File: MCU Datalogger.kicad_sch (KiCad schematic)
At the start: 25 parts, among them U1 24LC1025, U2 24LC1025, U3 DS1337S_, U4 ATMEGA328P-AU, Y1 16 MHz, Y2 32.768kHz

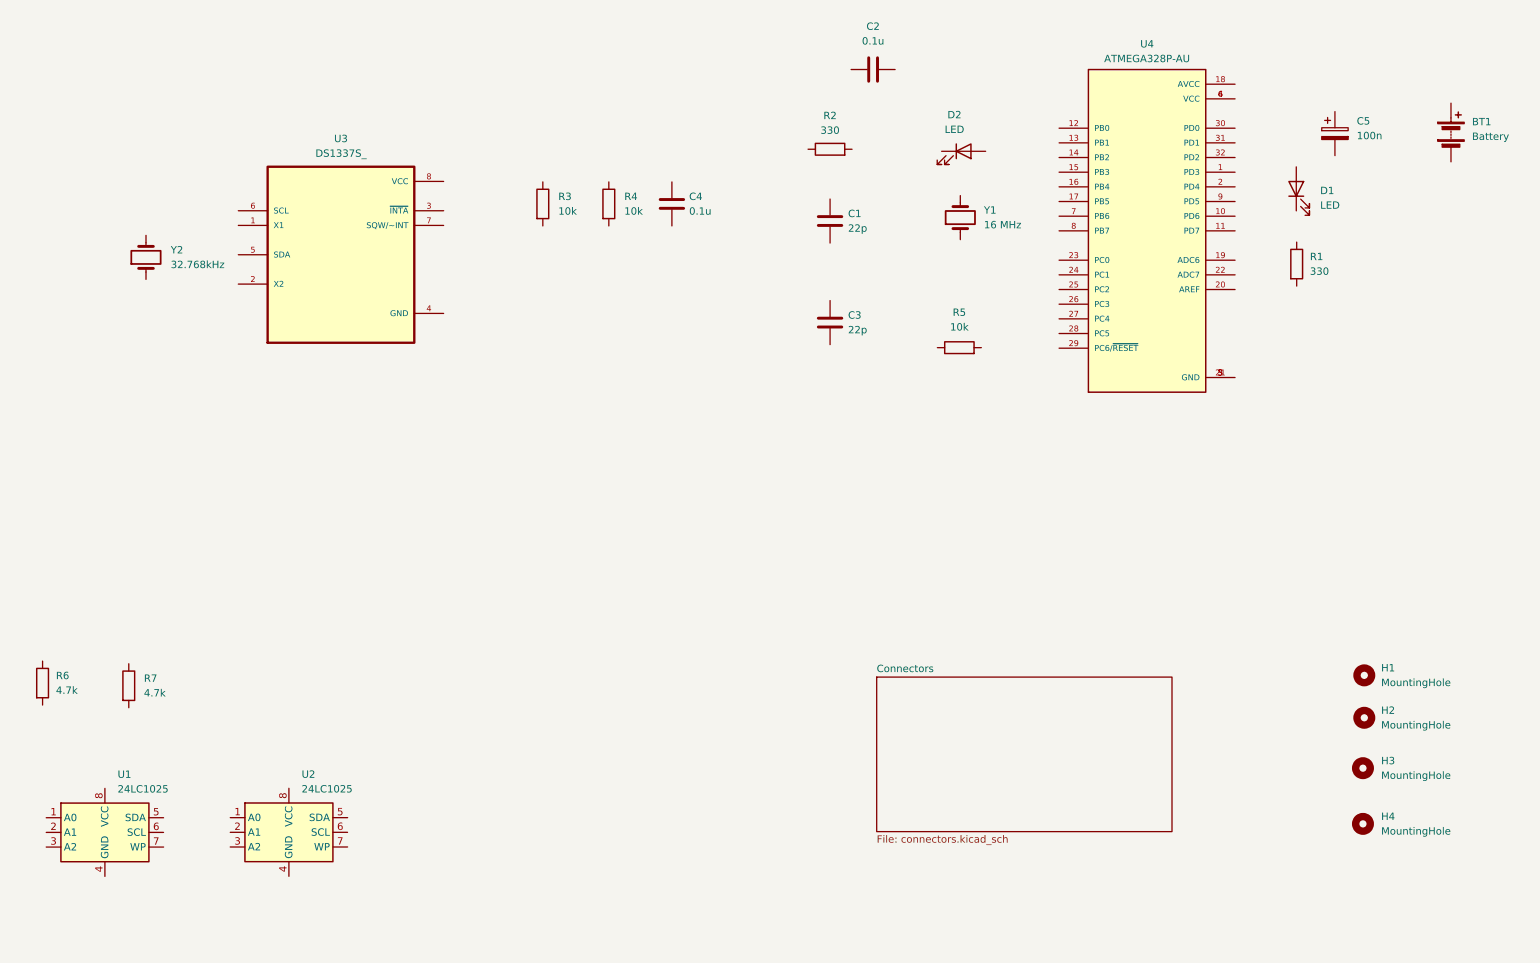
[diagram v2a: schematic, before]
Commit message: completed wiring of main sheet
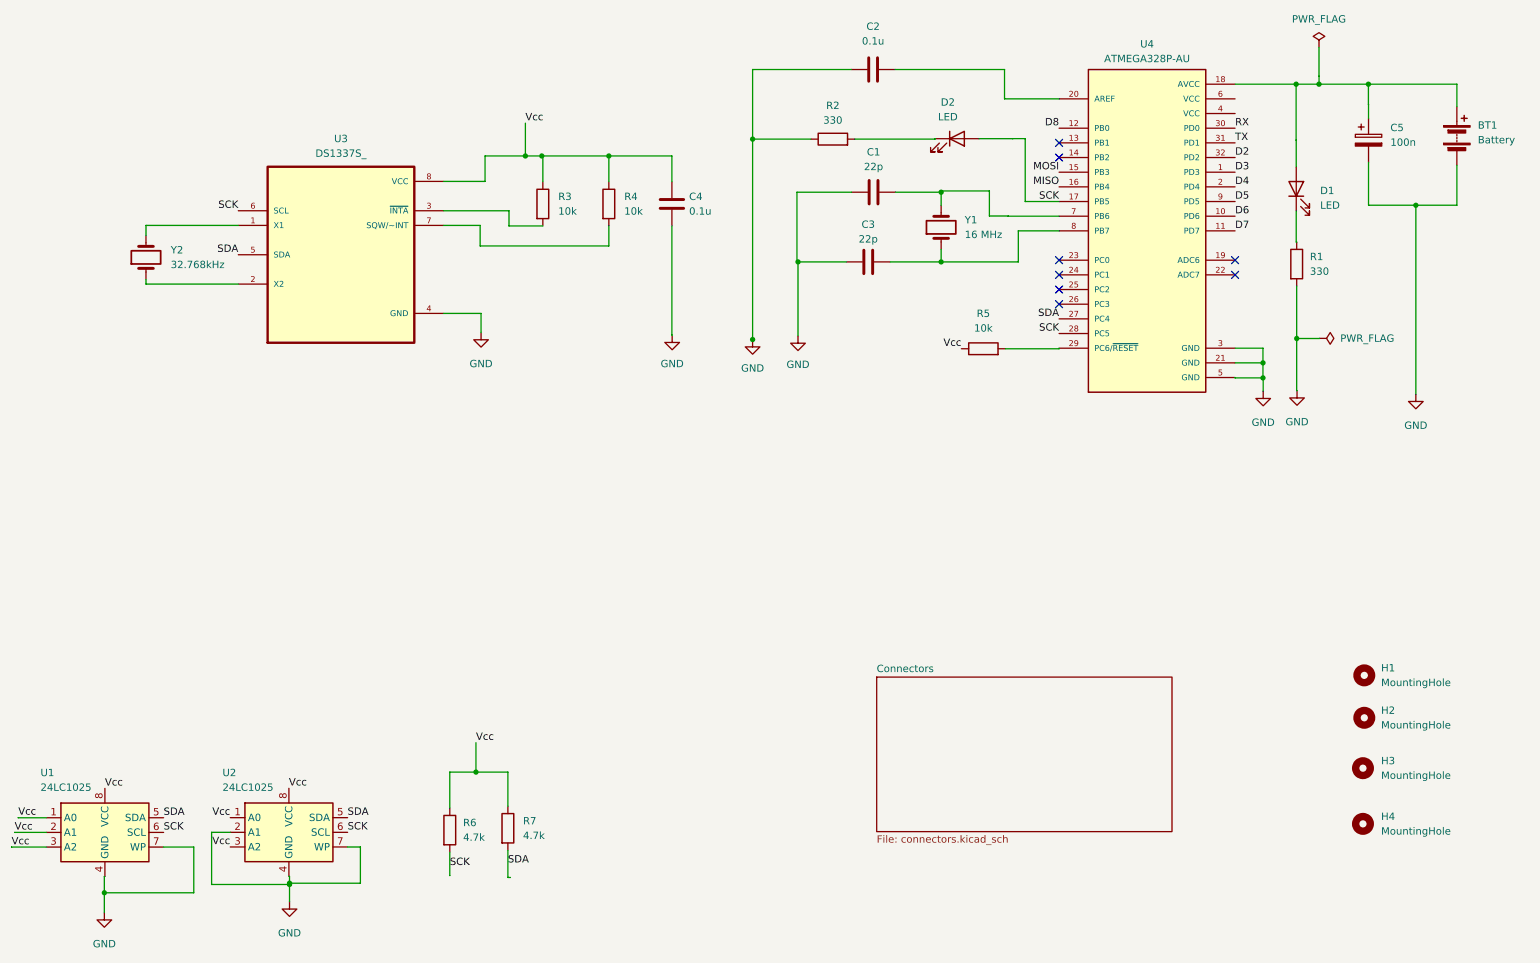
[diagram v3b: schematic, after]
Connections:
- net Vcc: now reaches R7.1
- net Vcc: now also C4.2, R3.1, R4.1, R5.1, R6.1, U1.1 (A0), U1.2 (A1), U1.3 (A2), U1.8 (VCC), U2.1 (A0), U2.3 (A2), U2.8 (VCC), U3.8 (VCC)
- net SDA: now reaches R7.2
- net SDA: now also U1.5 (SDA), U2.5 (SDA), U3.5 (SDA), U4.27 (PC4)
- net at R3.2: now also U3.3 (~{INTA})
- net GND: now reaches C1.1
- net GND: now also BT1.2 (-), C2.1, C3.1, C4.1, C5.2, R1.2, R2.1, U1.4 (GND), U1.7 (WP), U2.2 (A1), U2.4 (GND), U2.7 (WP), U3.4 (GND), U4.3 (GND), U4.5 (GND)
- net at C1.2: now also U4.7 (PB6), Y1.2
- net at C5.1: now also BT1.1 (+), D1.2 (A), U4.18 (AVCC)
- net at R1.1: now also D1.1 (K)
- net at R2.2: now also D2.1 (K)
- net SCK: now reaches U2.6 (SCL)
- net SCK: now also D2.2 (A), R6.2, U1.6 (SCL), U3.6 (SCL), U4.17 (PB5), U4.28 (PC5)
- net at R4.2: now also U3.7 (SQW/~INT)
- net at C3.2: now also U4.8 (PB7), Y1.1
- net at R5.2: now also U4.29 (PC6/~{RESET})
- net at C2.2: now also U4.20 (AREF)
- net at U3.1 (X1): now also Y2.2
- net at U3.2 (X2): now also Y2.1
- net D3: now reaches U4.1 (PD3)
- net D6: now reaches U4.10 (PD6)
- net D7: now reaches U4.11 (PD7)
- net D8: now reaches U4.12 (PB0)
- net MOSI: now reaches U4.15 (PB3)
- net MISO: now reaches U4.16 (PB4)
- net D4: now reaches U4.2 (PD4)
- net RX: now reaches U4.30 (PD0)
- net TX: now reaches U4.31 (PD1)
- net D2: now reaches U4.32 (PD2)
- net at U4.4 (VCC): no longer U4.6 (VCC)
- net D5: now reaches U4.9 (PD5)
- now unconnected: U4.21 (GND)
- no-connect marks 0 -> 8
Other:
- moved on the sheet: BT1, C1, C3, C5, D2, R2, R5, R6, R7, Y1

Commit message: Completed wiring in schematic
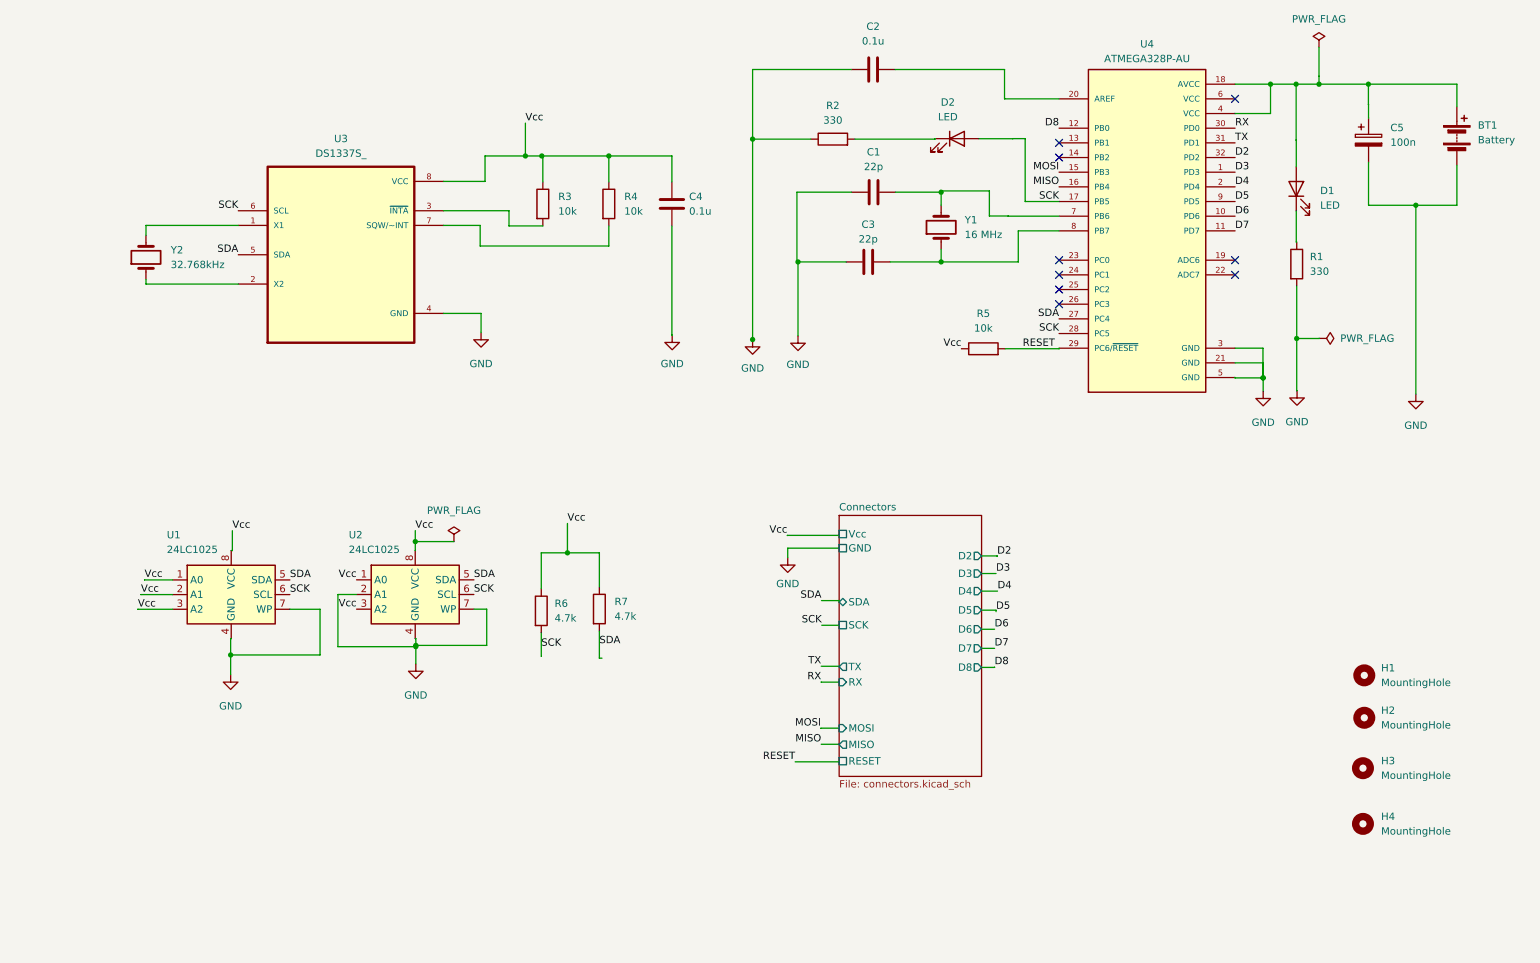
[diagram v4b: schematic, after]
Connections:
- net GND: now also U4.21 (GND)
- net at BT1.1 (+), C5.1, D1.2 (A)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: now also U4.4 (VCC)
- net RESET: now reaches R5.2, U4.29 (PC6/~{RESET})
- no-connect marks 8 -> 9
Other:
- sheet Connectors ports: added D2, D3, D4, D5, D6, D7, D8, GND, MISO, MOSI, RESET, RX, SCK, SDA, TX, Vcc; removed none
- moved on the sheet: R6, R7, U1, U2

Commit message: Added auxilary comments and graphics for better documenting
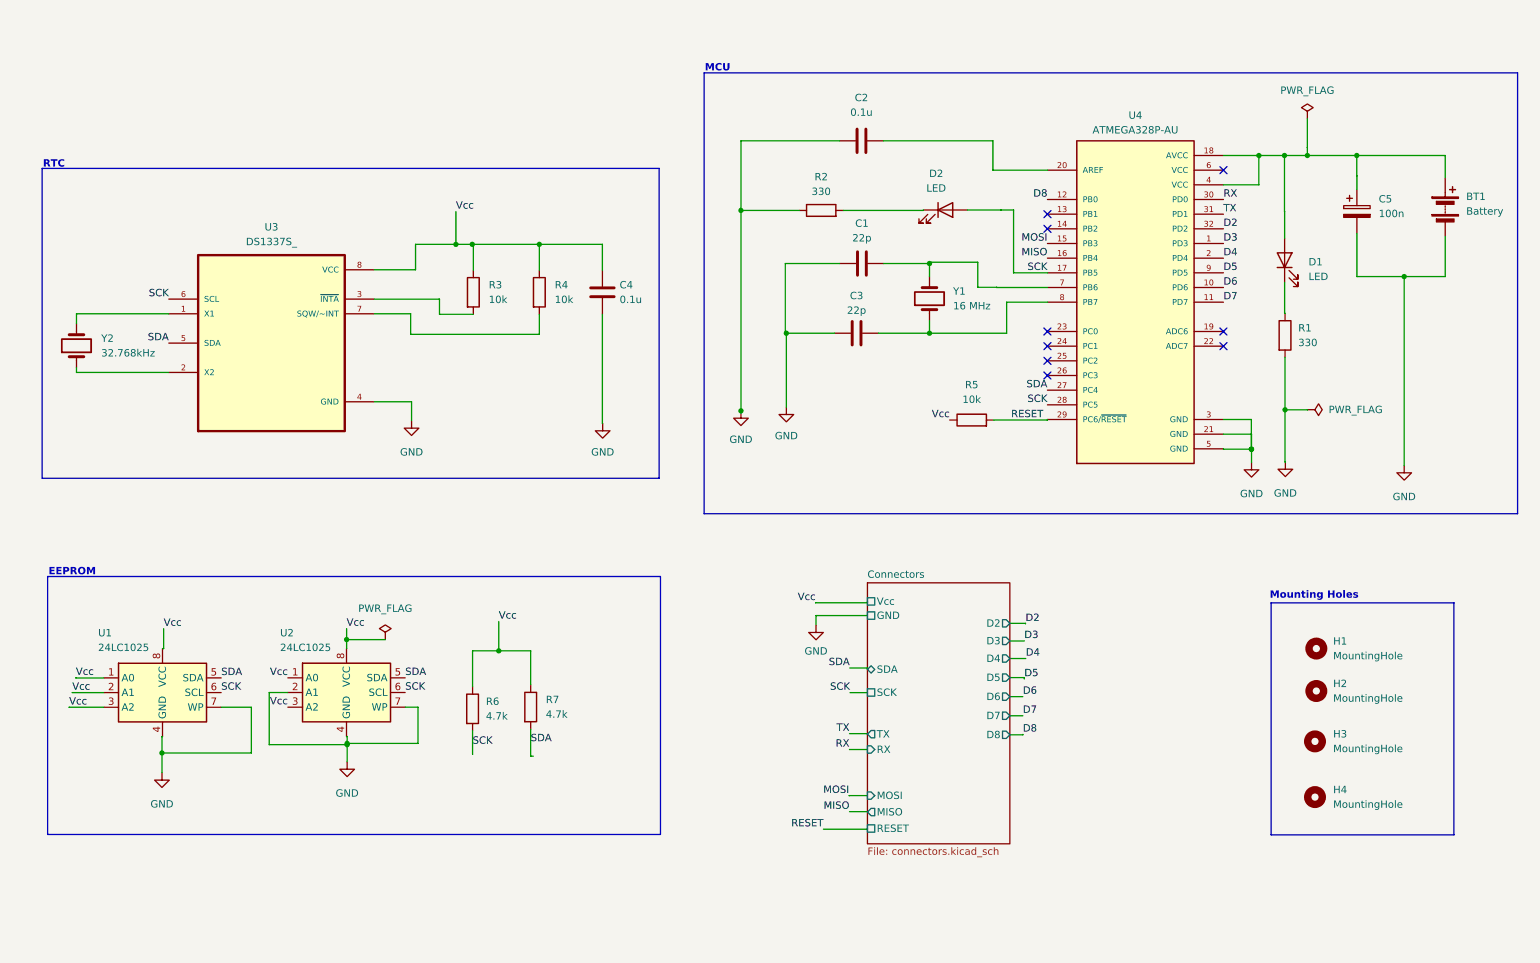
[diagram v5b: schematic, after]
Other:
- note added: "EEPROM"
- note added: "MCU"
- note added: "Mounting Holes"
- note added: "RTC"
- moved on the sheet: BT1, C1, C2, C3, C4, C5, D1, D2, H1, H2, H3, H4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

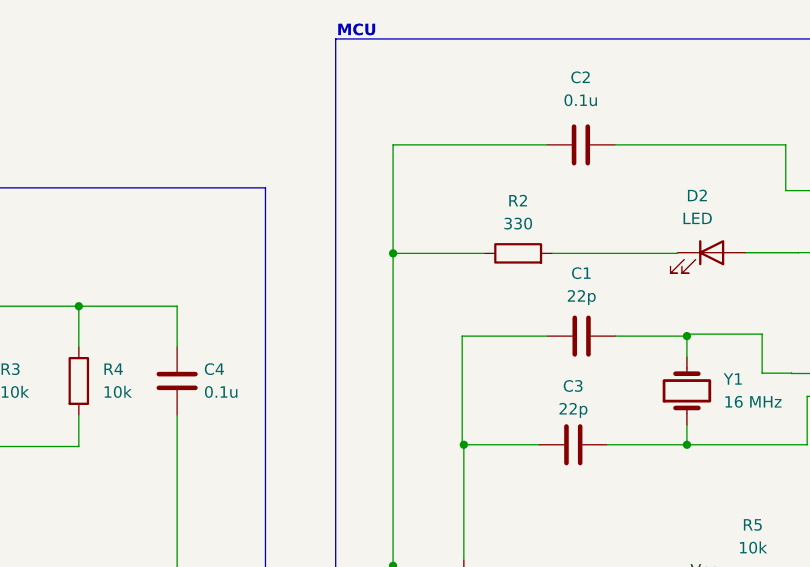
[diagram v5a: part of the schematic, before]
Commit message: completed placement of footprints
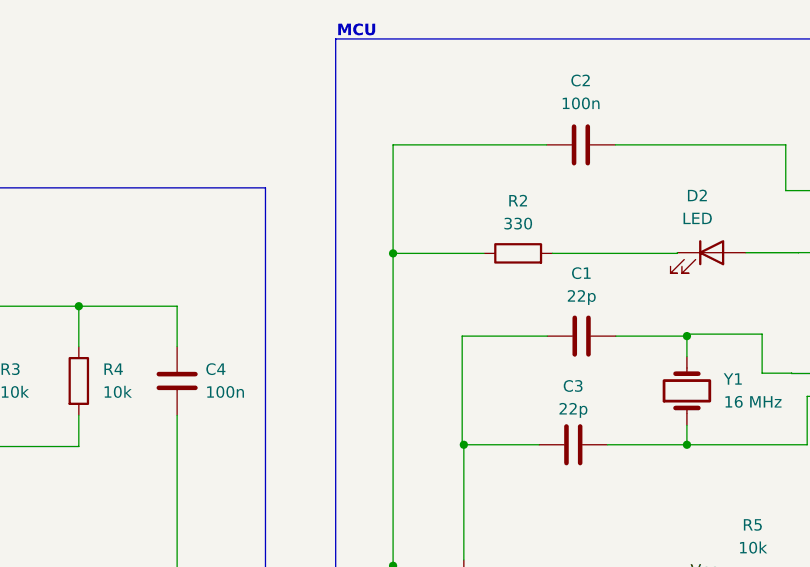
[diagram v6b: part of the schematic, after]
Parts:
- C2, C4: value 0.1u -> 100n
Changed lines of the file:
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@@
   (symbol (lib_id "Device:C") (at 122.5834 66.3573 180) (unit 1)
     (in_bom yes) (on_board yes) (dnp no) (fields_autoplaced)
-    (property "Reference" "C4" (at 125.5637 65.0873 0)
+    (property "Reference" "C4" (at 125.73 65.0873 0)
       (effects (font (size 1.27 1.27)) (justify right))
     )
-    (property "Value" "0.1u" (at 125.5637 67.6273 0)
+    (property "Value" "100n" (at 125.73 67.6273 0)
       (effects (font (size 1.27 1.27)) (justify right))
     )
@@
   (symbol (lib_id "Device:C") (at 167.4492 40.1239 90) (unit 1)
     (in_bom yes) (on_board yes) (dnp no) (fields_autoplaced)
-    (property "Reference" "C2" (at 167.4492 32.6692 90)
+    (property "Reference" "C2" (at 167.4492 33.02 90)
       (effects (font (size 1.27 1.27)))
     )
-    (property "Value" "0.1u" (at 167.4492 35.2092 90)
+    (property "Value" "100n" (at 167.4492 35.56 90)
       (effects (font (size 1.27 1.27)))
     )

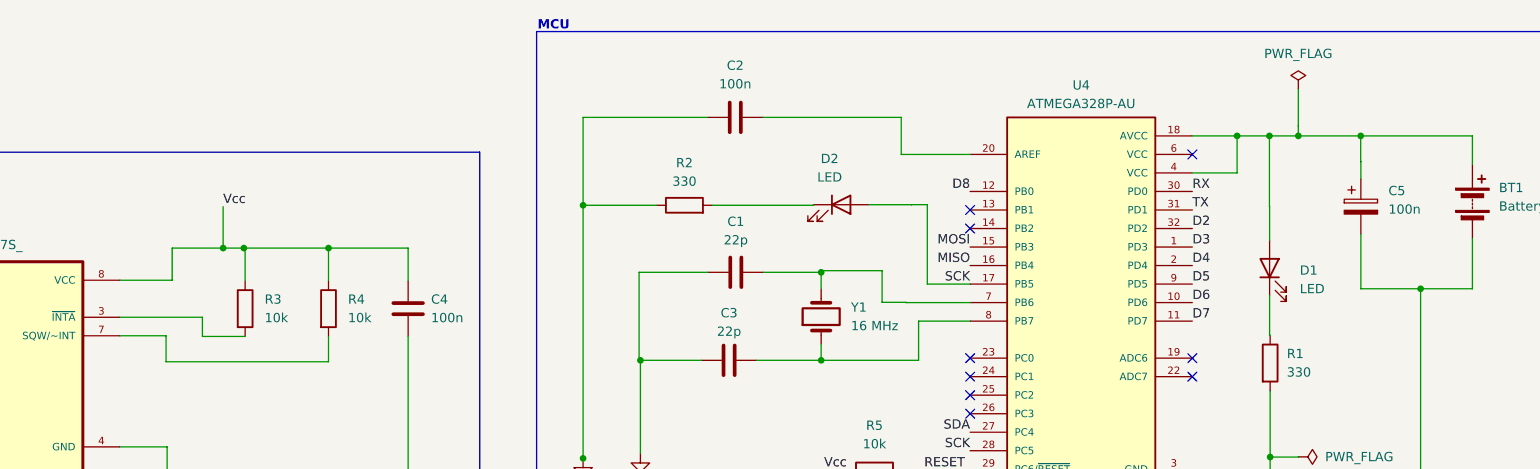
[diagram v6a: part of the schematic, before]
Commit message: Routing completed, PWR zones added, DRC checked
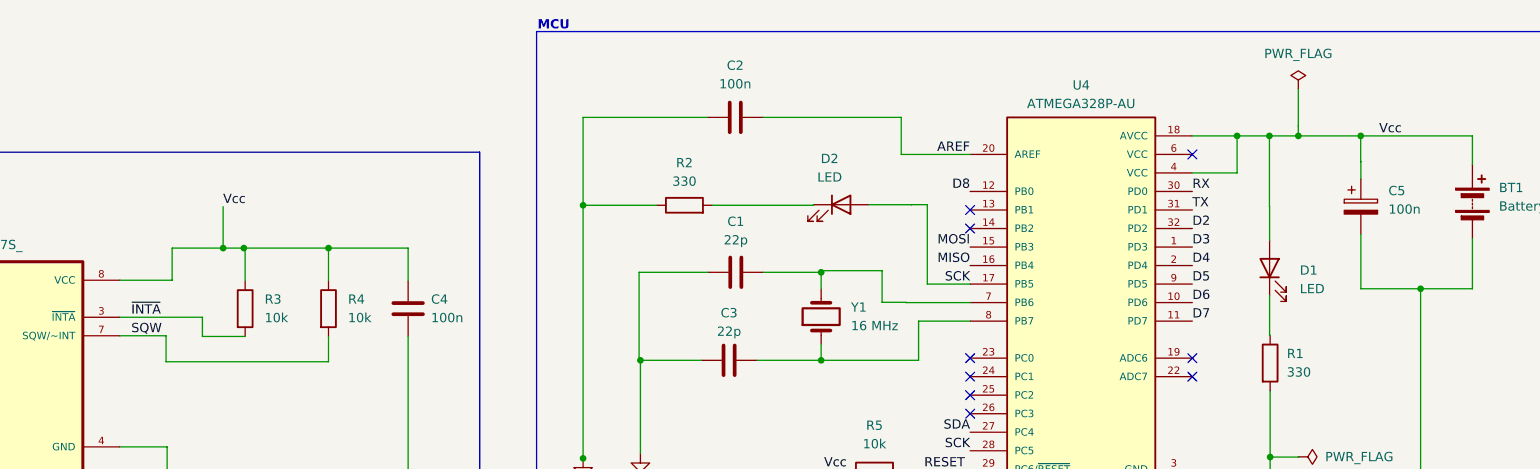
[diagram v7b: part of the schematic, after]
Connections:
- net Vcc: now also BT1.1 (+), C5.1, D1.2 (A), U4.18 (AVCC), U4.4 (VCC)
- net ~{INTA}: now reaches R3.2, U3.3 (~{INTA})
- net SQW: now reaches R4.2, U3.7 (SQW/~INT)
- net AREF: now reaches C2.2, U4.20 (AREF)
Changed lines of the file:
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@@
+    (effects (font (size 1.27 1.27)) (justify left bottom))
+  )
+  (label "Vcc" (at 255.752 42.666 0) (fields_autoplaced)
     (effects (font (size 1.27 1.27)) (justify left bottom))
   )
@@
     (effects (font (size 1.27 1.27)) (justify left bottom))
   )
+  (label "SQW" (at 84.6086 70.0771 0) (fields_autoplaced)
+    (effects (font (size 1.27 1.27)) (justify left bottom))
+  )
+  (label "~{INTA}" (at 84.6086 67.5371 0) (fields_autoplaced)
+    (effects (font (size 1.27 1.27)) (justify left bottom))
+  )
   (label "Vcc" (at 182.7328 88.4827 180) (fields_autoplaced)
     (effects (font (size 1.27 1.27)) (justify right bottom))
@@
     (effects (font (size 1.27 1.27)) (justify right bottom))
   )
+  (label "AREF" (at 195.1353 45.206 0) (fields_autoplaced)
+    (effects (font (size 1.27 1.27)) (justify left bottom))
+  )
   (label "D8" (at 199.6547 50.286 180) (fields_autoplaced)
